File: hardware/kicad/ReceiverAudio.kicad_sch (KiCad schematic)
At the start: 118 parts, among them J10 Headphones, J4 Conn_01x03, J5 Audio Gain, J6 Audio Out, J7 Speaker, J8 Conn_01x04, J9 Conn_01x02, Q4 J177, Q5 2N3904, Q6 2N3904, Q7 VN10LF, Q8 VN10LF, U10 LM386, U7 TS924, U8 TS924, U9 OPA1641

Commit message: Firmware: encoder ISR queue, S-meter calibration, UI polish, SI5351 fixes
Firmware changes:
- RotaryInput: rewrite to interrupt-driven ISR queue (RP2040 GPIO callback,
  64-event ring buffer). Eliminates ~2-3 step/sec polling limit.
- SI5351Control: add liveRetune param to setQuadrature90(). Live-retune path
  skips PLL reset and output disable/enable to eliminate audio transients.
  Both CLK0/CLK1 forced to PLLA for phase coherence. Phase registers zeroed
  in all low-band paths.
- BoardControl: S-meter ADC inversion (higher V = weaker signal), configurable
  zero-raw floor, gain permille, and optional sqrt log companding.
- main.cpp: analogReadResolution(12) for 12-bit ADC. S_METER_ZERO_RAW=372
  (~3V floor), GAIN=1220, LOG=true. Tune coalescing via flushPendingTuneDelta.
  40ms display refresh throttle. S-meter suppressed during tuning (120ms).
  LED steady on (no heartbeat). SI5351 correction -4610000 PPB.
- DisplayUI: step indicator label, flashTuneDirection (UP/DN), step digit
  flash with 500ms duration on encoder button press.
- upload_uf2.py: wait-for-mount loop + picotool fallback upload.

Hardware:
- KiCAD PCB and schematic updates (mixer sheet, audio sheet)
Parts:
- C92: footprint Capacitor_SMD:CP_Elec_3x5.3 -> Capacitor_SMD:CP_Elec_6.3x4.9
- D3, D4: footprint Diode_SMD:D_0805_2012Metric -> Diode_SMD:D_1206_3216Metric
- D5: footprint Inductor_SMD:L_0805_2012Metric -> Diode_SMD:D_1206_3216Metric
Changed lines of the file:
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@@
 			)
 		)
-		(property "Footprint" "Diode_SMD:D_0805_2012Metric"
+		(property "Footprint" "Diode_SMD:D_1206_3216Metric"
 			(at 262.89 36.83 0)
 			(effects
@@
 			)
 		)
-		(property "Footprint" "Inductor_SMD:L_0805_2012Metric"
+		(property "Footprint" "Diode_SMD:D_1206_3216Metric"
 			(at 262.89 69.85 0)
 			(effects
@@
 			)
 		)
-		(property "Footprint" "Diode_SMD:D_0805_2012Metric"
+		(property "Footprint" "Diode_SMD:D_1206_3216Metric"
 			(at 151.13 179.07 0)
 			(effects
@@
 			)
 		)
-		(property "Footprint" "Capacitor_SMD:CP_Elec_3x5.3"
+		(property "Footprint" "Capacitor_SMD:CP_Elec_6.3x4.9"
 			(at 142.24 157.48 0)
 			(effects

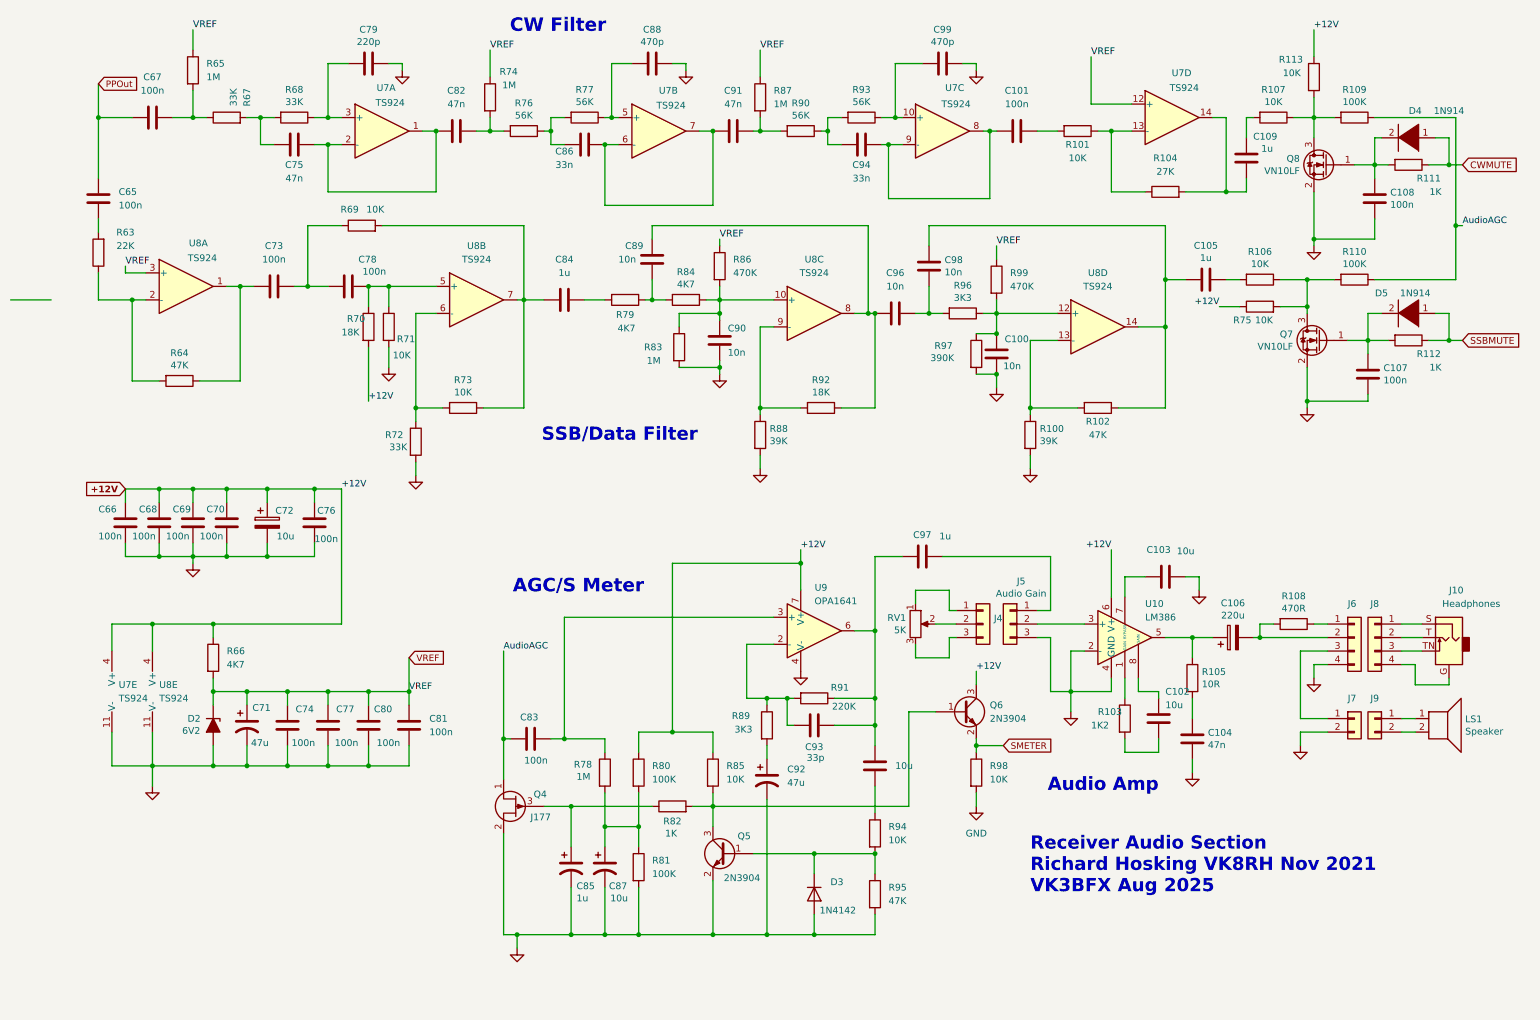
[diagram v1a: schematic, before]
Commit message: Fixed quadrature generation PCB excirt circuit in draft
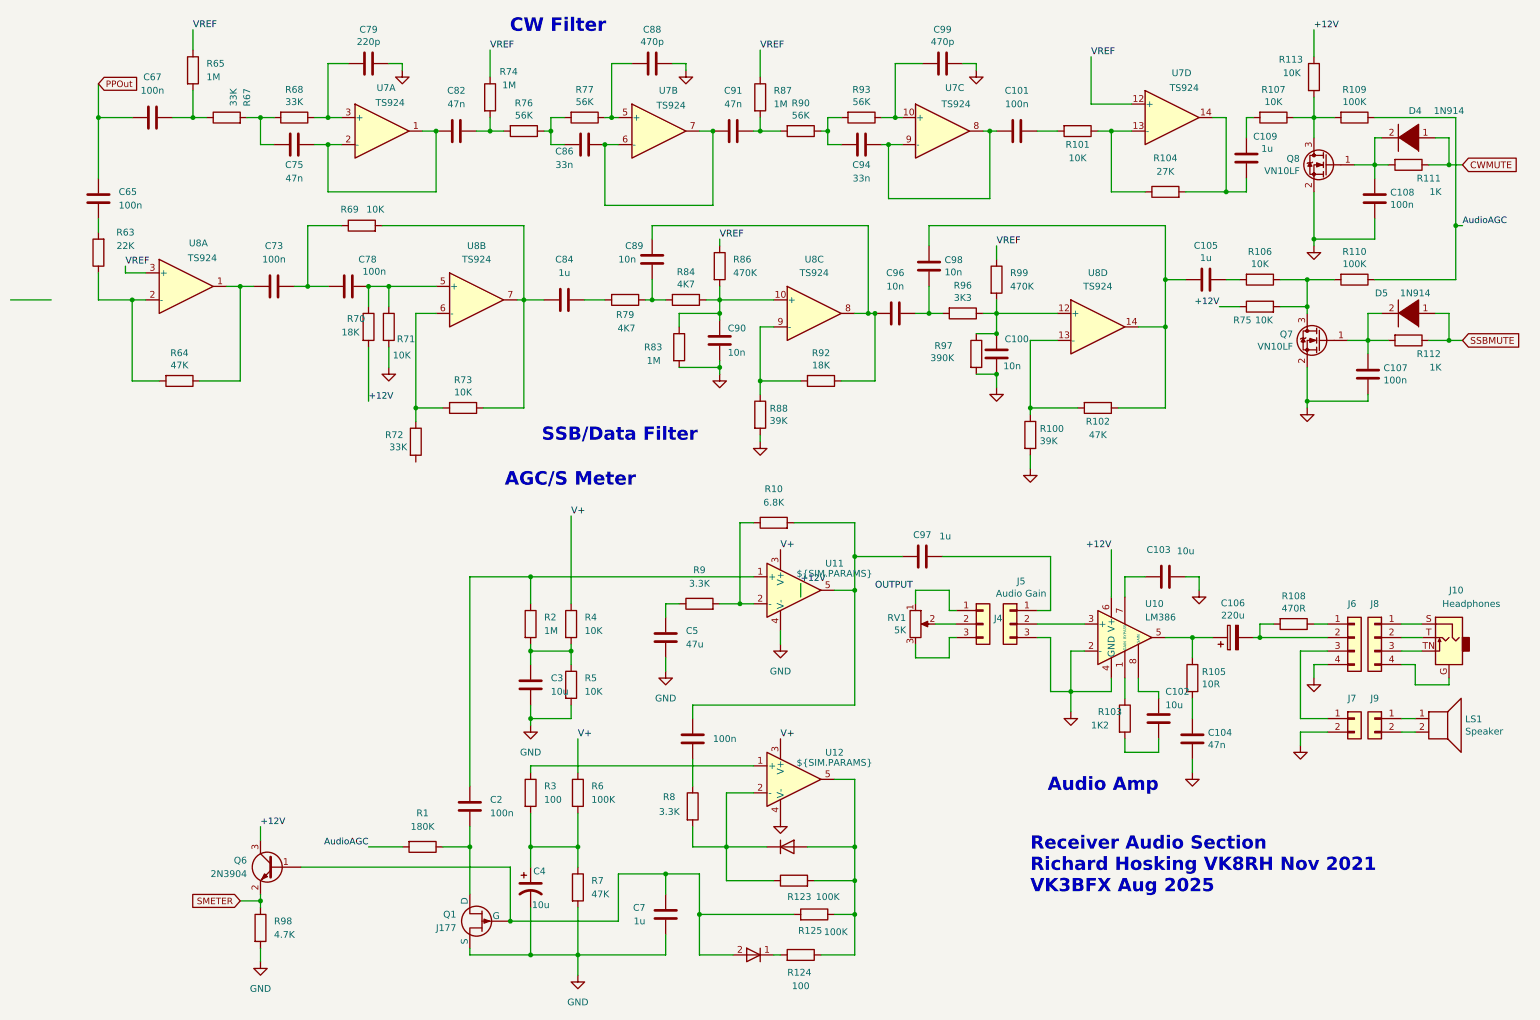
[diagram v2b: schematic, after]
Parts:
- removed C66, C68, C69, C70, C74, C76, C77, C80, C81, C83: 100n, Capacitor_SMD:C_0805_2012Metric, symbol Device:C
- removed C71: 47u, Capacitor_SMD:CP_Elec_3x5.3, symbol Device:C_Polarized_US
- removed C72: 10u, Capacitor_SMD:C_1206_3216Metric, symbol QRPTransceiver-rescue:CP-Device
- removed C85: 1u, Capacitor_SMD:C_1206_3216Metric, symbol Device:C_Polarized_US
- removed C87: 10u, Capacitor_SMD:CP_Elec_3x5.3, symbol Device:C_Polarized_US
- removed C92: 47u, Capacitor_SMD:CP_Elec_6.3x4.9, symbol Device:C_Polarized_US
- removed C93: 33p, Capacitor_SMD:C_0805_2012Metric, symbol Device:C
- removed C95: 10u, Capacitor_SMD:CP_Elec_3x5.3, symbol Device:C
- removed D2: 6V2, Diode_SMD:D_0805_2012Metric, symbol Device:D_Zener_Filled
- removed D3: 1N4142, Diode_SMD:D_1206_3216Metric, symbol Device:D
- removed Q4: J177, Package_TO_SOT_SMD:SC-59, symbol Device:Q_PJFET_DGS
- removed Q5: 2N3904, Package_TO_SOT_SMD:SOT-23, symbol Transistor_BJT:2N3904
- removed R66: 4K7, Resistor_SMD:R_0805_2012Metric, symbol Device:R
- removed R78: 1M, Resistor_SMD:R_0805_2012Metric, symbol Device:R
- removed R80, R81: 100K, Resistor_SMD:R_0805_2012Metric, symbol Device:R
- removed R82: 1K, Resistor_SMD:R_0805_2012Metric, symbol Device:R
- removed R85, R94: 10K, Resistor_SMD:R_0805_2012Metric, symbol Device:R
- removed R89: 3K3, Resistor_SMD:R_0805_2012Metric, symbol Device:R
- removed R91: 220K, Resistor_SMD:R_0805_2012Metric, symbol Device:R
- removed R95: 47K, Resistor_SMD:R_0805_2012Metric, symbol Device:R
- removed unit 5 of U7
- removed unit 5 of U8
- removed U9: OPA1641, Package_SO:SO-8_3.9x4.9mm_P1.27mm, symbol Amplifier_Operational:OPA1641
- added C2, C8: 100n, symbol Device:C
- added C3: 10u, symbol Device:C
- added C4: 10u, symbol Device:C_Polarized_US
- added C5: 47u, symbol Device:C
- added C7: 1u, symbol Device:C
- added D6: D, symbol Simulation_SPICE:D
- added D7: D, symbol Device:D
- added Q1: J177, symbol Simulation_SPICE:PJFET
- added R1: 180K, symbol Device:R
- added R10: 6.8K, symbol Device:R
- added R123, R125, R6: 100K, symbol Device:R
- added R124, R3: 100, symbol Device:R
- added R2: 1M, symbol Device:R
- added R4, R5: 10K, symbol Device:R
- added R7: 47K, symbol Device:R
- added R8, R9: 3.3K, symbol Device:R
- added U11, U12: ${SIM.PARAMS}, symbol Simulation_SPICE:OPAMP
- R98: value 10K -> 4.7K
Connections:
- net AudioAGC: now also R1.2
- net GND: now also C3.2, C4.2, C5.2, C7.2, Q1.3 (S), R5.2, R7.2, U11.4 (V-), U12.4 (V-); no longer R72.2
- net at C97.1: now also C8.1, R10.2, U11.5
- net at Q6.1: now also C7.1, D6.2 (A), Q1.2 (G), R125.2
- new net: C8.2, R8.1
- new net: D7.1 (K), R123.1, R8.2, U12.2 (-)
- new net: D6.1 (K), R124.2
- new net: C3.1, R2.2, R4.2, R5.1
- new net: D7.2 (A), R123.2, R124.1, R125.1, U12.5
- new net: C2.1, R2.1, U11.1 (+)
- new net: R10.1, R9.2, U11.2 (-)
- new net: R3.1, U12.1 (+)
- new net: C5.1, R9.1
- new net: C4.1, R3.2, R6.2, R7.1
- new net: C2.2, Q1.1 (D), R1.1
- new net V+: R4.1, R6.1, U11.3 (V+), U12.3 (V+)
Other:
- moved on the sheet: Q6, R88, R92, R98

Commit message: Document SSC notes reference in CURRENT_SI5351_APPROACH.md
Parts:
- U10: renamed from U12; value ${SIM.PARAMS} -> ~
- U9: renamed from U11; value ${SIM.PARAMS} -> ~
- renumbered C106 to C100, C109 to C101, C107 to C102, C108 to C103, C65 to C70, C67 to C71, C73 to C72, C75 to C73, C78 to C74, C79 to C75, C82 to C76, C2 to C77, C3 to C78, C4 to C79, C84 to C80, C86 to C81, C88 to C82, C89 to C83, C5 to C84, C7 to C85, C8 to C86, C90 to C87, C91 to C88, C94 to C89, C96 to C90, C97 to C91, C98 to C92, C99 to C93, C100 to C94, C101 to C95, C102 to C96, C103 to C97, C104 to C98, C105 to C99, D6 to D1, D7 to D2, D4 to D3, D5 to D4, J4 to J3, J5 to J4, J6 to J5, J7 to J6, J8 to J7, J9 to J8, J10 to J9, Q6 to Q5, Q1 to Q6, R6 to R100, R7 to R101, R77 to R102, R79 to R103, R83 to R104, R84 to R105, R8 to R106, R9 to R107, R86 to R108, R87 to R109, R88 to R110, R10 to R111, R123 to R112, R90 to R113, R124 to R114, R125 to R115, R92 to R116, R93 to R117, R96 to R118, R97 to R119, R99 to R120, R100 to R121, R101 to R122, R102 to R123, R103 to R124, R104 to R125, R105 to R126, R106 to R127, R75 to R128, R107 to R129, R108 to R130, R113 to R131, R109 to R132, R110 to R133, R111 to R134, R112 to R135, R63 to R82, R64 to R83, R65 to R84, R67 to R85, R98 to R86, R68 to R87, R69 to R88, R70 to R89, R71 to R90, R72 to R91, R1 to R92, R73 to R93, R74 to R94, R76 to R95, R2 to R96, R3 to R97, R4 to R98, R5 to R99, RV1 to RV2, U10 to U11, U8 to U7, U7 to U8
